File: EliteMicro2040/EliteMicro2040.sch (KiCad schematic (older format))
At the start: 52 parts, among them J2 SKRKAEE020, J5 Conn_01x03_Male, U1 TLV75533PDBVR, U2 Elite-C, U3 RP2040, Y1 3225_4P

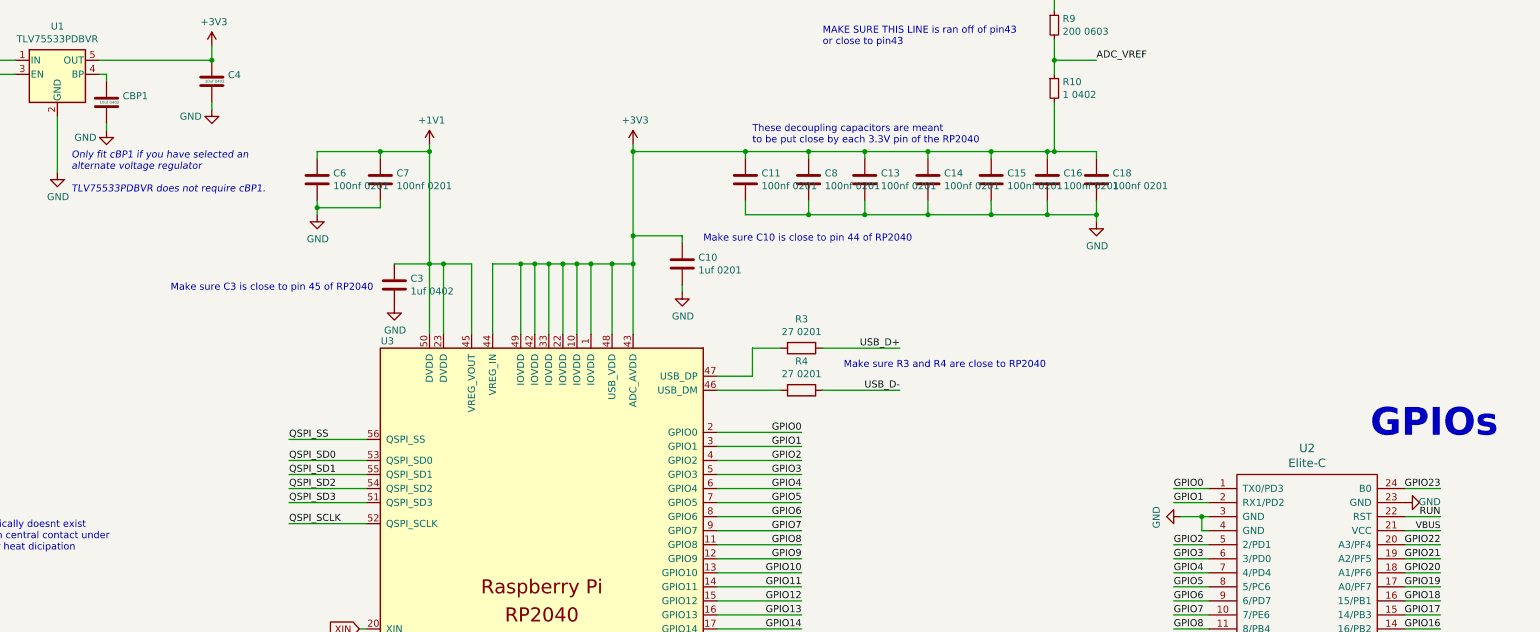
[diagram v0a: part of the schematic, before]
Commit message: moved some parts about to fit optional bypass resistor
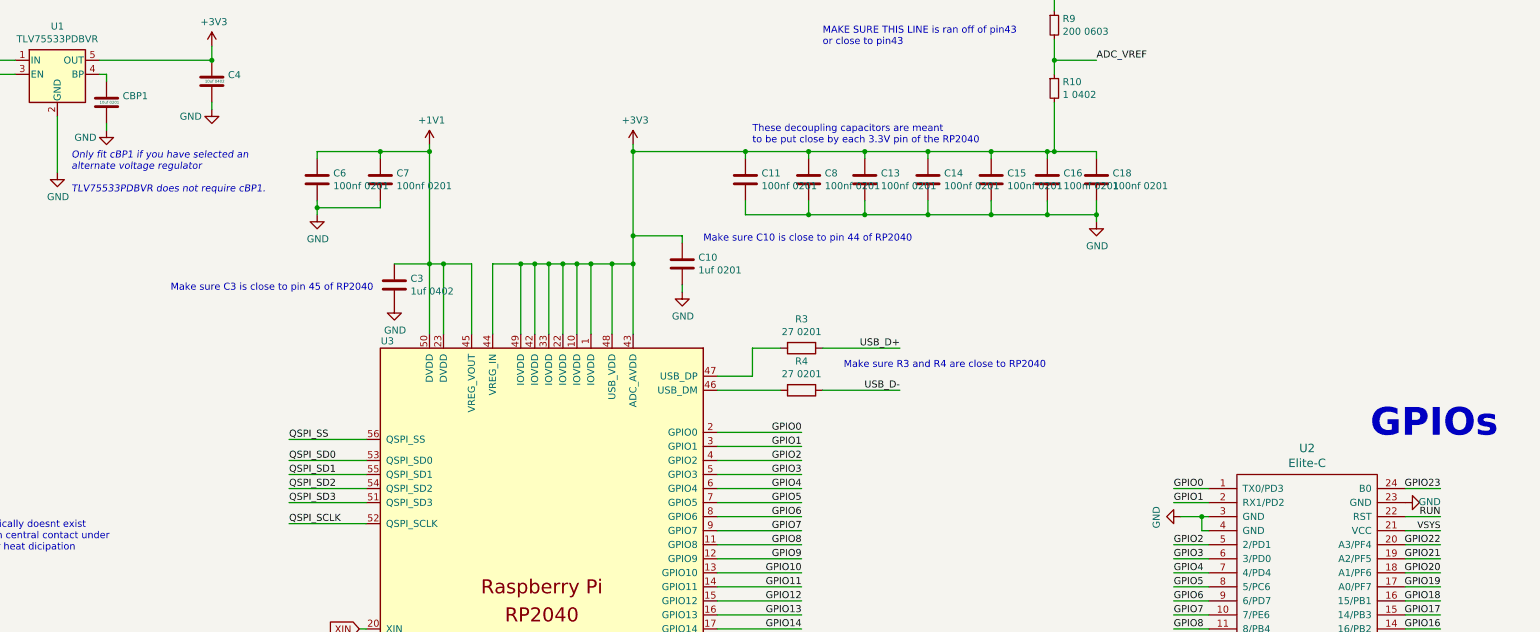
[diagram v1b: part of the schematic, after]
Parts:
- CBP1: value 10uf 0402 -> 10uf 0201; footprint Capacitor_SMD:C_0402_1005Metric -> Capacitor_SMD:C_0201_0603Metric
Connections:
- net VBUS: no longer U2.21 (VCC)
- net VSYS: now also U2.21 (VCC)
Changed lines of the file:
@@
 P 4700 2050
 F 0 "CBP1" H 4815 2096 50  0000 L CNN
-F 1 "10uf 0402" H 4650 2050 20  0000 L CNN
-F 2 "Capacitor_SMD:C_0402_1005Metric" H 4738 1900 50  0001 C CNN
+F 1 "10uf 0201" H 4650 2050 20  0000 L CNN
+F 2 "Capacitor_SMD:C_0201_0603Metric" H 4738 1900 50  0001 C CNN
 F 3 "" H 4700 2050 50  0001 C CNN
 F 4 " " H 4700 2050 50  0001 C CNN "LCSC"
@@
 VBUS
 Text Label 14200 5100 2    47   ~ 0
-VBUS
+VSYS
 Wire Wire Line
 	12300 5300 12550 5300

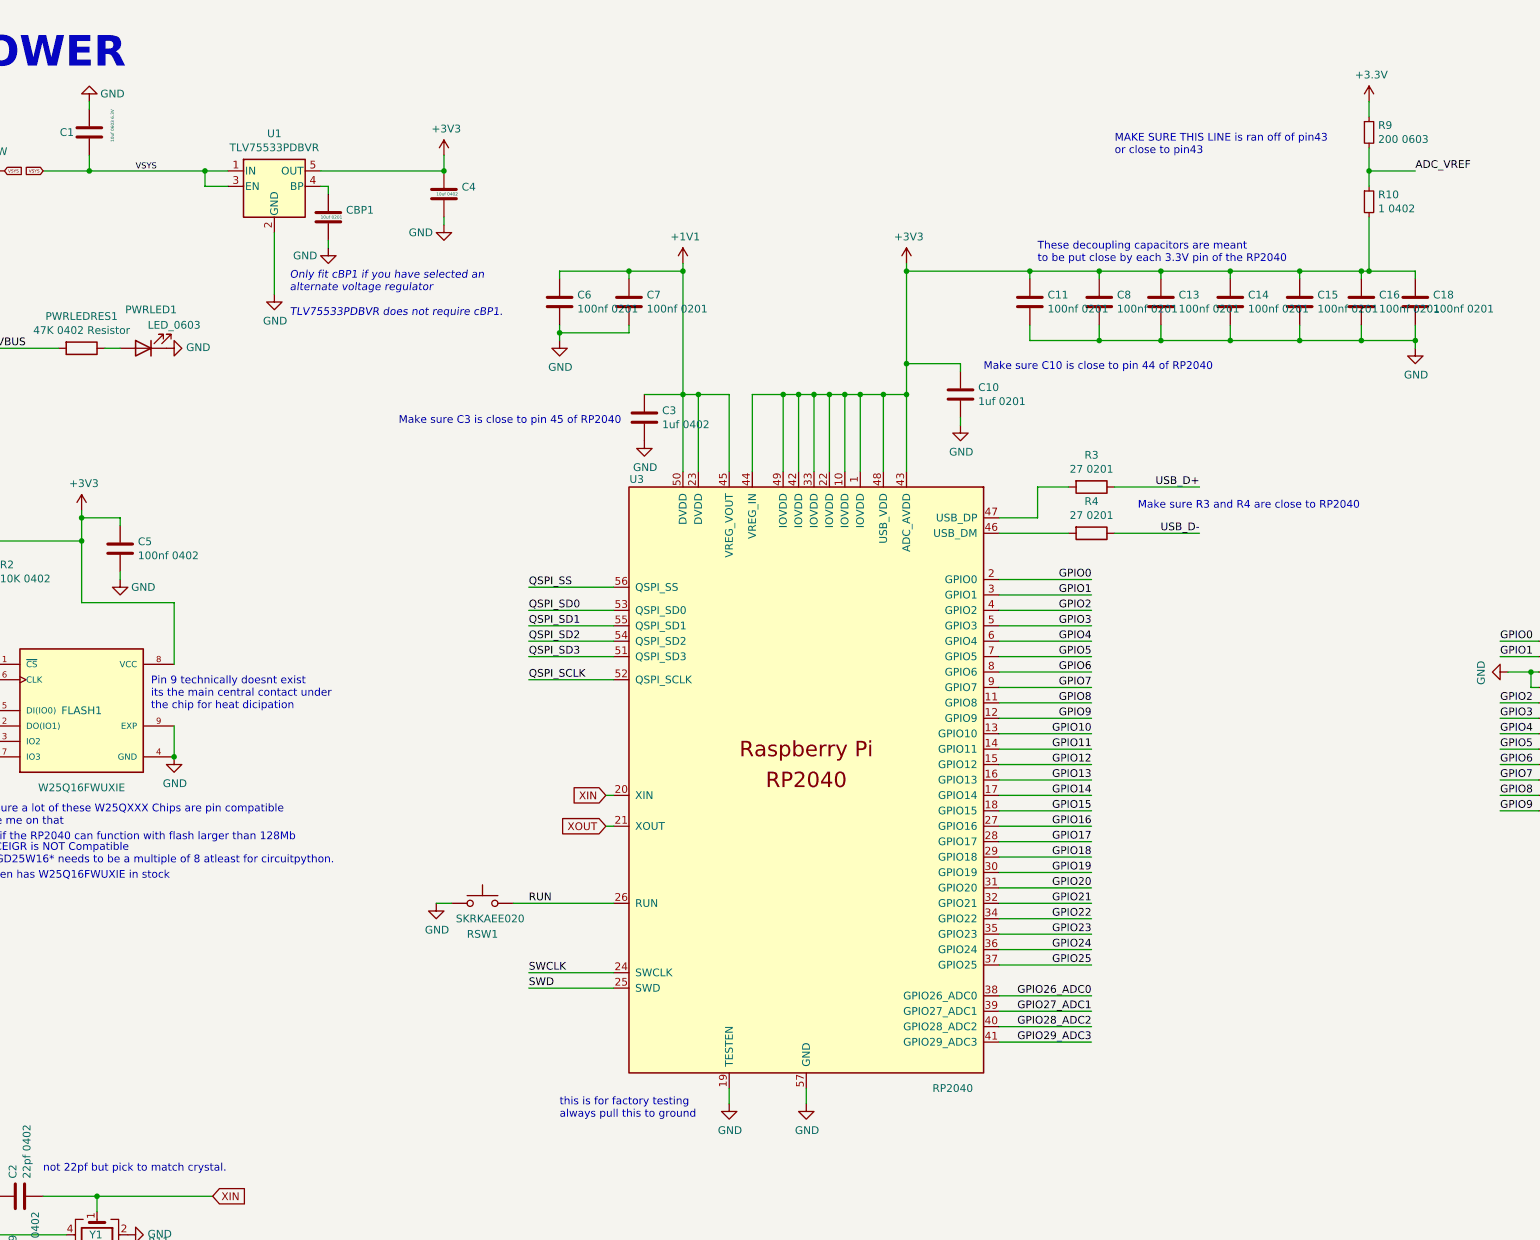
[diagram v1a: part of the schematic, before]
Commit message: shortened pcb, added bypass resistor, pads for SPI flash and supporting decoupling capacitor
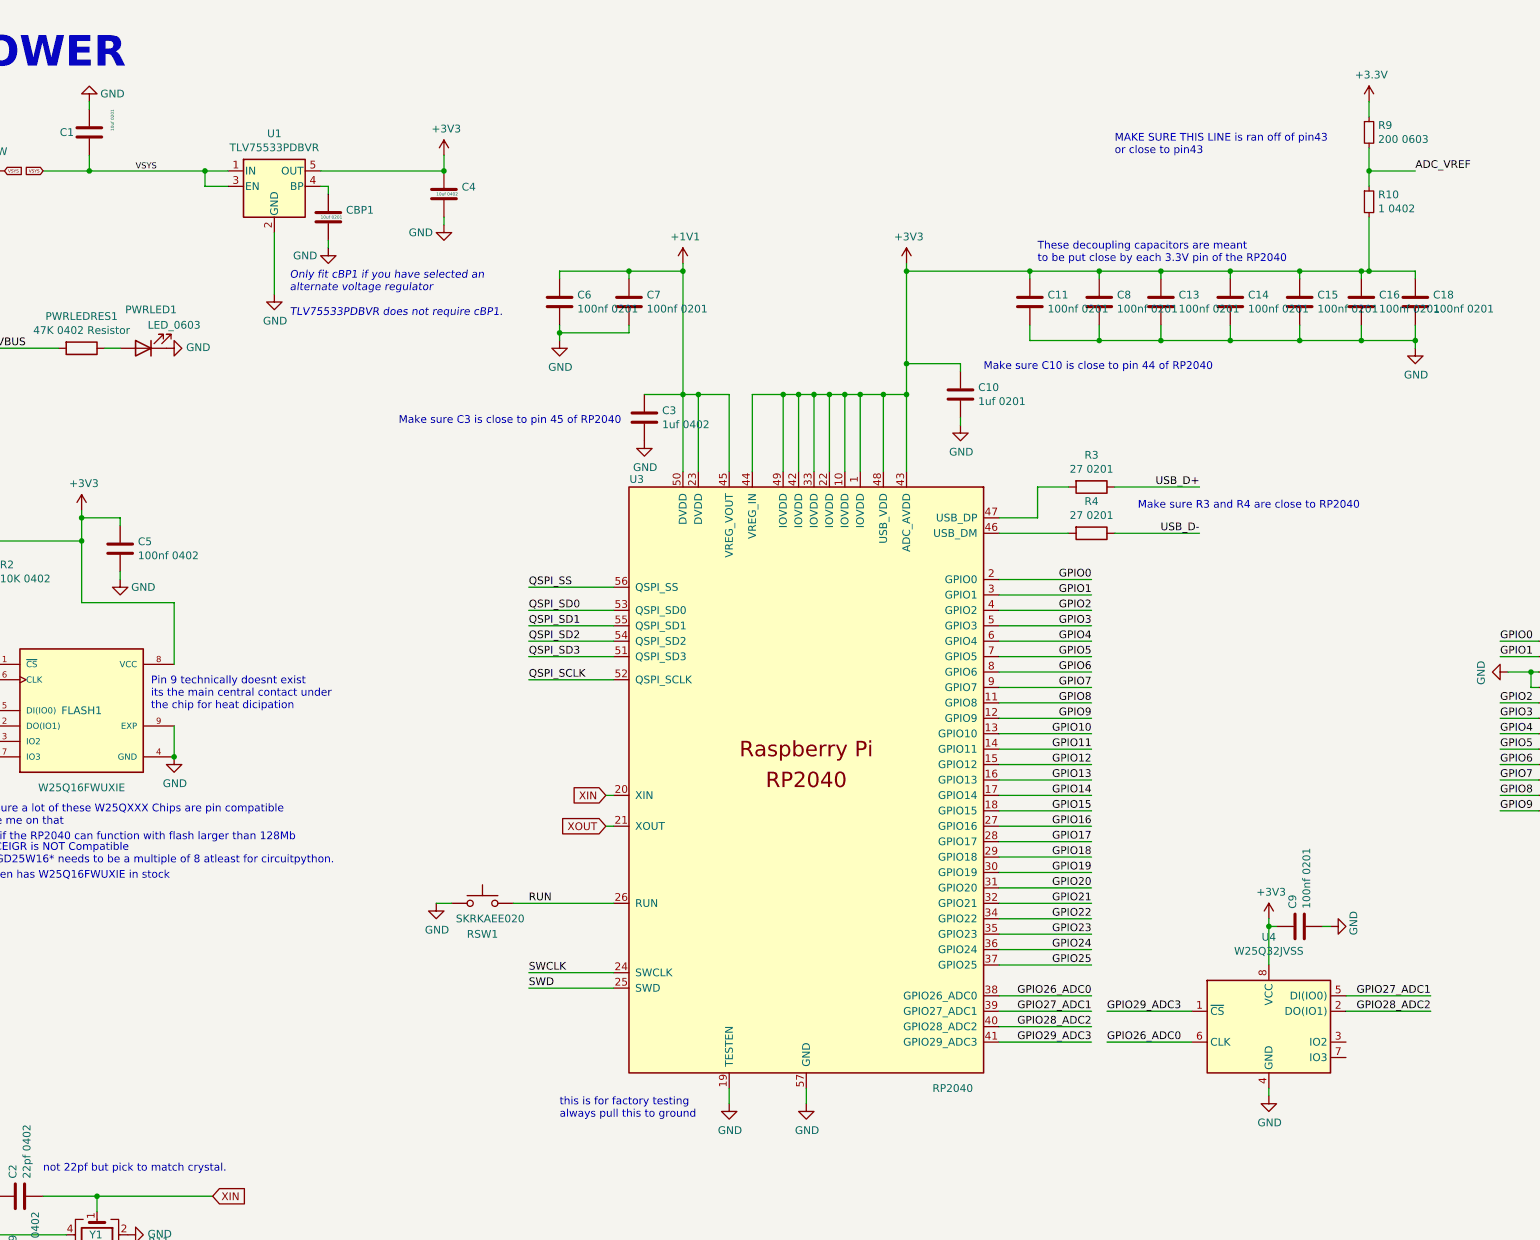
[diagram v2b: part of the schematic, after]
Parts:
- added C9: 100nf 0201, Capacitor_SMD:C_0201_0603Metric, symbol Device:C
- added U4: W25Q32JVSS, Package_SON:SON-8-1EP_3x2mm_P0.5mm_EP1.4x1.6mm, symbol Memory_Flash:W25Q32JVSS
- C1: value 10uf 0603 6.3V -> 10uf 0201; footprint Capacitor_SMD:C_0603_1608Metric -> Capacitor_SMD:C_0201_0603Metric
- D1: footprint Diode_SMD:D_SOD-123 -> Diode_SMD:D_SOD-323
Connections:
- net +3V3: now also C9.1, U4.8 (VCC)
- net GND: now also C9.2, U4.4 (GND)
- net GPIO26_ADC0: now also U4.6 (CLK)
- net GPIO27_ADC1: now also U4.5 (DI(IO0))
- net GPIO28_ADC2: now also U4.2 (DO(IO1))
- net GPIO29_ADC3: now also U4.1 (~CS)
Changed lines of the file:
@@
 	9050 7400 9650 7400
-$Comp
-L power:GND #PWR016
-U 1 1 5EDC82DF
-P 7800 7800
-F 0 "#PWR016" H 7800 7550 50  0001 C CNN
-F 1 "GND" H 7805 7627 50  0000 C CNN
-F 2 "" H 7800 7800 50  0001 C CNN
-F 3 "" H 7800 7800 50  0001 C CNN
-	1    7800 7800
-	1    0    0    -1
-$EndComp
 $Comp
 L power:GND #PWR015
@@
 	2500 4500 2500 4950
 Wire Wire Line
-	3350 4350 3350 4400
-Wire Wire Line
 	2500 4150 3100 4150
 Wire Wire Line
@@
 F 3 "" H 3350 4400 50  0001 C CNN
 	1    3350 4400
-	1    0    0    -1
-$EndComp
-$Comp
-L Device:C C5
-U 1 1 5EDB1AA1
-P 3350 4200
-F 0 "C5" H 3465 4246 50  0000 L CNN
-F 1 "100nf 0402" H 3465 4155 50  0000 L CNN
-F 2 "Capacitor_SMD:C_0402_1005Metric" H 3388 4050 50  0001 C CNN
-F 3 "" H 3350 4200 50  0001 C CNN
-F 4 " " H 3350 4200 50  0001 C CNN "LCSC"
-	1    3350 4200
 	1    0    0    -1
 $EndComp
@@
 P 3150 1500
 F 0 "C1" H 3250 1500 50  0000 L CNN
-F 1 "10uf 0603 6.3V" V 3000 1350 20  0000 L CNN
-F 2 "Capacitor_SMD:C_0603_1608Metric" H 3188 1350 50  0001 C CNN
+F 1 "10uf 0201" V 3000 1350 20  0000 L CNN
+F 2 "Capacitor_SMD:C_0201_0603Metric" H 3188 1350 50  0001 C CNN
 F 3 "" H 3150 1500 50  0001 C CNN
 F 4 " " H 3150 1500 50  0001 C CNN "LCSC"
@@
 F 0 "D1" H 2450 1533 50  0000 C CNN
 F 1 "1N4002W" H 2450 1624 50  0000 C CNN
-F 2 "Diode_SMD:D_SOD-123" H 2450 1750 50  0001 C CNN
+F 2 "Diode_SMD:D_SOD-323" H 2450 1750 50  0001 C CNN
 F 3 "" H 2450 1750 50  0001 C CNN
 F 4 " " H 2450 1750 50  0001 C CNN "LCSC"
@@
 Wire Wire Line
 	3900 1750 4050 1750
+$Comp
+L Device:C C5
+U 1 1 5EDB1AA1
+P 3350 4200
+F 0 "C5" H 3465 4246 50  0000 L CNN
+F 1 "100nf 0402" H 3465 4155 50  0000 L CNN
+F 2 "Capacitor_SMD:C_0402_1005Metric" H 3388 4050 50  0001 C CNN
+F 3 "" H 3350 4200 50  0001 C CNN
+F 4 " " H 3350 4200 50  0001 C CNN "LCSC"
+	1    3350 4200
+	1    0    0    -1
+$EndComp
+Wire Wire Line
+	3350 4350 3350 4400
+$Comp
+L Device:C C9
+U 1 1 61B67544
+P 11000 6650
+F 0 "C9" H 11115 6696 50  0000 L CNN
+F 1 "100nf 0201" H 11115 6605 50  0000 L CNN
+F 2 "Capacitor_SMD:C_0201_0603Metric" H 11038 6500 50  0001 C CNN
+F 3 "" H 11000 6650 50  0001 C CNN
+F 4 " " H 11000 6650 50  0001 C CNN "LCSC"
+	1    11000 6650
+	0    -1   -1   0
+$EndComp
+$Comp
+L power:GND #PWR0104
+U 1 1 61B83F9C
+P 11200 6650
+F 0 "#PWR0104" H 11200 6400 50  0001 C CNN
+F 1 "GND" H 11300 6500 50  0000 R CNN
+F 2 "" H 11200 6650 50  0001 C CNN
+F 3 "" H 11200 6650 50  0001 C CNN
+	1    11200 6650
+	0    -1   -1   0
+$EndComp
+Wire Wire Line
+	11200 6650 11150 6650
+$Comp
+L Memory_Flash:W25Q32JVSS U4
+U 1 1 61B5790C
+P 10800 7300
+F 0 "U4" H 10800 7881 50  0000 C CNN
+F 1 "W25Q32JVSS" H 10800 7790 50  0000 C CNN
+F 2 "Package_SON:SON-8-1EP_3x2mm_P0.5mm_EP1.4x1.6mm" H 10800 7300 50  0001 C CNN
+F 3 "http://www.winbond.com/resource-files/w25q32jv%20revg%2003272018%20plus.pdf" H 10800 7300 50  0001 C CNN
+	1    10800 7300
+	1    0    0    -1
+$EndComp
+$Comp
+L power:+3V3 #PWR0111
+U 1 1 61BCC9BB
+P 10800 6600
+F 0 "#PWR0111" H 10800 6450 50  0001 C CNN
+F 1 "+3V3" H 10815 6773 50  0000 C CNN
+F 2 "" H 10800 6600 50  0001 C CNN
+F 3 "" H 10800 6600 50  0001 C CNN
+	1    10800 6600
+	1    0    0    -1
+$EndComp
+Wire Wire Line
+	10850 6650 10800 6650
+Wire Wire Line
+	10800 6650 10800 6600
+Wire Wire Line
+	10800 6650 10800 6900
+Connection ~ 10800 6650
+$Comp
+L power:GND #PWR016
+U 1 1 5EDC82DF
+P 7800 7800
+F 0 "#PWR016" H 7800 7550 50  0001 C CNN
+F 1 "GND" H 7805 7627 50  0000 C CNN
+F 2 "" H 7800 7800 50  0001 C CNN
+F 3 "" H 7800 7800 50  0001 C CNN
+	1    7800 7800
+	1    0    0    -1
+$EndComp
+$Comp
+L power:GND #PWR0117
+U 1 1 61BF774B
+P 10800 7750
+F 0 "#PWR0117" H 10800 7500 50  0001 C CNN
+F 1 "GND" H 10805 7577 50  0000 C CNN
+F 2 "" H 10800 7750 50  0001 C CNN
+F 3 "" H 10800 7750 50  0001 C CNN
+	1    10800 7750
+	1    0    0    -1
+$EndComp
+Wire Wire Line
+	10800 7750 10800 7700
+Text Label 9750 7400 0    50   ~ 0
+GPIO26_ADC0
+Wire Wire Line
+	9750 7400 10300 7400
+Text Label 9750 7200 0    50   ~ 0
+GPIO29_ADC3
+Wire Wire Line
+	9750 7200 10300 7200
+Text Label 11850 7100 2    50   ~ 0
+GPIO27_ADC1
+Wire Wire Line
+	11850 7100 11300 7100
+Text Label 11850 7200 2    50   ~ 0
+GPIO28_ADC2
+Wire Wire Line
+	11300 7200 11850 7200
 $EndSCHEMATC

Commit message: Lots of changes, redid elite-c version, added more debug pads to main version and various tweaks among other things.
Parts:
- removed D1: 1N4002W, Diode_SMD:D_SOD-323, symbol Device:D_Schottky
- removed H1, H2, H3, H4: MountingHole, MountingHole:MountingHole_2.2mm_M2, symbol Mechanical:MountingHole
- removed PWRLED1: LED_0603, LED_SMD:LED_0603_1608Metric, symbol Device:LED
- removed PWRLEDRES1: 47K 0402 Resistor, Resistor_SMD:R_0402_1005Metric, symbol Device:R
- removed R10: 1 0402, Resistor_SMD:R_0402_1005Metric, symbol Device:R_Small
- removed R9: 200 0603, Resistor_SMD:R_0603_1608Metric, symbol Device:R_Small
- removed TP5, TP6, TP7, TP8: TestPoint, TestPoint:TestPoint_Pad_D1.0mm, symbol Connector:TestPoint
- J2, RSW1: footprint Button_Switch_SMD:SW_Push_SPST_NO_Alps_SKRK -> Jumper:SolderJumper-2_P1.3mm_Bridged_Pad1.0x1.5mm
- TP1, TP2, TP3, TP4: footprint TestPoint:TestPoint_Pad_D1.0mm -> EnvExtras:CustomTestPoint
- USB1: value TYPE-C-31-M-12 -> TYPE-C-31-M-14; footprint HRO-TYPE-C31-M-12:HRO-TYPE-C-31-M-12 -> josh-connectors:USB_C_TYPE-C-31-M-14; symbol Type-C:HRO-TYPE-C-31-M-12 -> josh-connector:USB_C_U262-161N-4BVC11
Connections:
- net VSYS is gone; now on net VBUS: C1.1, U1.1 (IN), U1.3 (EN), U2.21 (VCC)
- net GND: now also USB1.A1 (GND), USB1.A12 (GND), USB1.B1 (GND), USB1.B12 (GND), USB1.S1 (SHIELD); no longer TP3.1, USB1.1 (GND), USB1.12 (GND), USB1.13 (SHIELD)
- net RUN: now also TP3.1
- net USB_D+: now also USB1.A6 (D+), USB1.B6 (D+); no longer USB1.6 (DP1), USB1.8 (DP2)
- net USB_D-: now also USB1.A7 (D-), USB1.B7 (D-); no longer USB1.5 (DN2), USB1.7 (DN1)
- net VBUS: now also USB1.A4 (VBUS), USB1.A9 (VBUS), USB1.B4 (VBUS), USB1.B9 (VBUS); no longer TP4.1, USB1.11 (VBUS), USB1.2 (VBUS)
- net ~USB_BOOT: now also TP4.1
- net at R6.2: now also USB1.B5 (CC2); no longer USB1.10 (CC2)
- net at R5.2: now also USB1.A5 (CC1); no longer USB1.4 (CC1)
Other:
- note removed: "2x 5.1K Resistors on the CC pins will = 5V@1.5A\nthis is the recomended default config for type-c"
- note removed: "KoreanHROParts \nUSB_C_Receptacle_HRO_TYPE-C-31-M-12"
- note removed: "MAKE SURE THIS LINE is ran off of pin43\nor close to pin43"
- note removed: "place one by the CPU\nand one by the regulator\n(3.3V Test points)"
- moved on the sheet: GPIO25_LED1, GPIO25_RESISTOR1
